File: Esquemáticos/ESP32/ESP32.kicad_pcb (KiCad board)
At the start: 2 copper layers, 100 x 100 mm, 71 parts, among them J1 Conector para bobinas del mot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, J2 Conector para bobinas del mot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, J3 Barrel_Jack, J4 USB Programador, Q1 S8550, Q2 S8550, Q3 S8550, Q4 S8550, Q5 S8550, Q6 S8550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

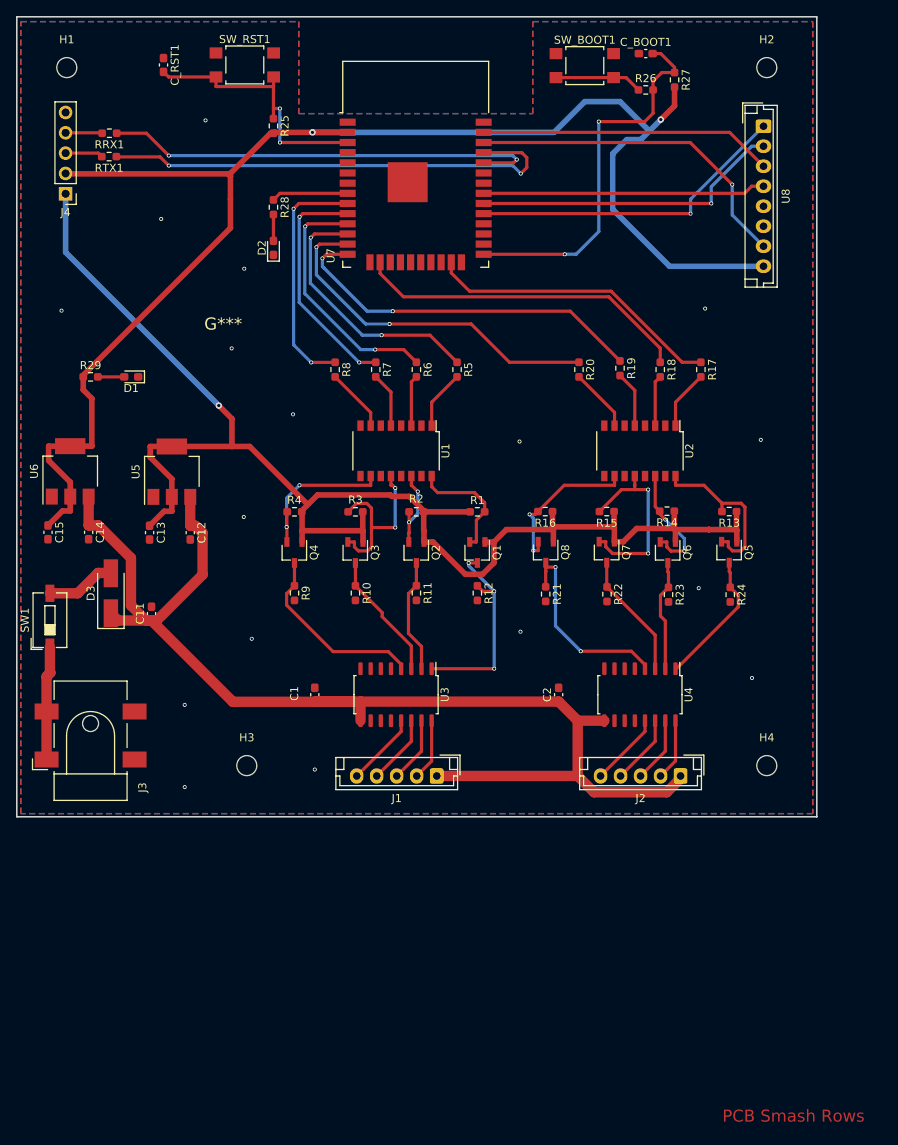
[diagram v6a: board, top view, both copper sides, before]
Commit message: Actualizada la PCB con impresiones de qué es cada pin de los conectores
Pendiente: Agregar capacitor de bypass en la entrada de 3v3 del ESP32 y listo, a comerciar con los chinos
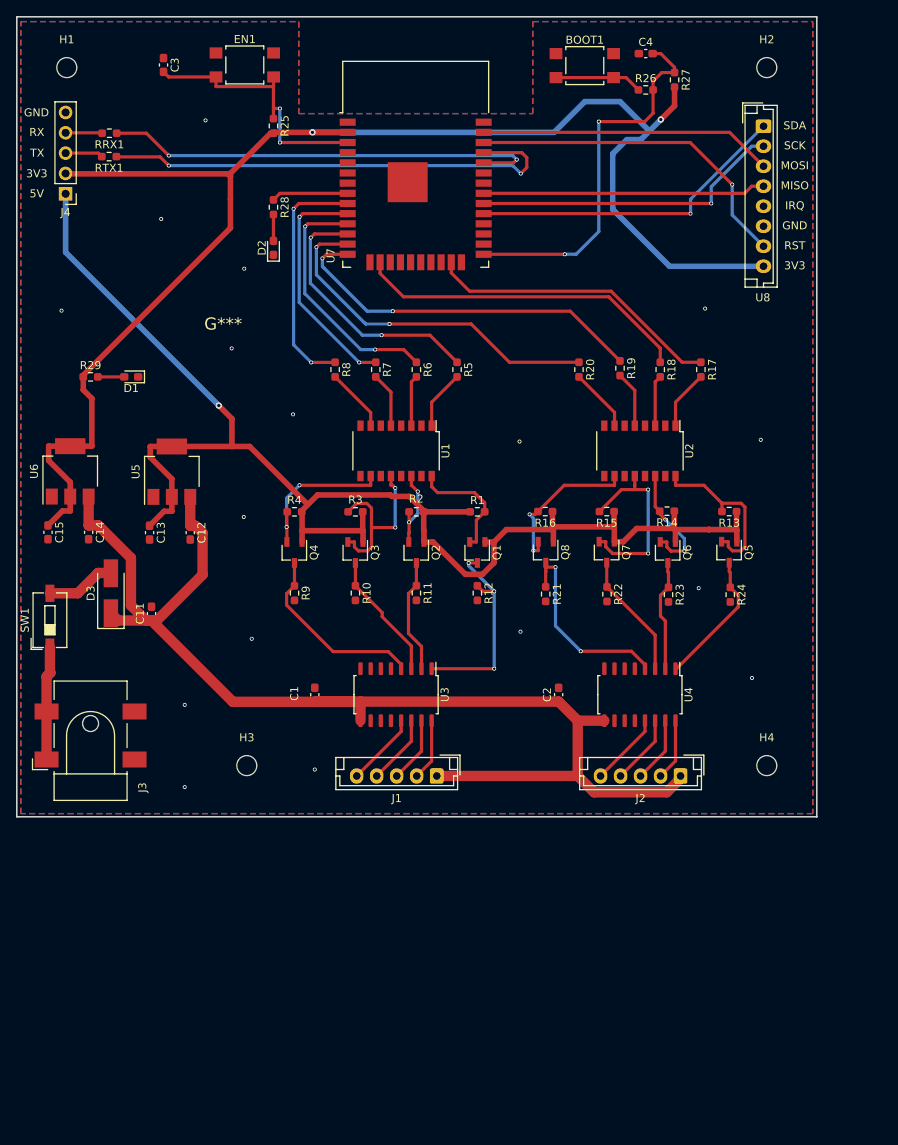
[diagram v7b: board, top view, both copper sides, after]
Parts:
- renumbered SW_BOOT1 to BOOT1, C_RST1 to C3, C_BOOT1 to C4, SW_RST1 to EN1
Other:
- board text added: "3V3"
- board text added: "5V"
- board text added: "GND"
- board text added: "IRQ"
- board text added: "MISO"
- board text added: "MOSI"
- board text added: "RST"
- board text added: "RX"
- board text added: "SCK"
- board text added: "SDA"
- board text added: "TX"
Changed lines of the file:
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@@
     (property "Sheetname" "RFID")
     (attr through_hole)
-    (fp_text reference "U8" (at 8.75 -2.8 90) (layer "F.SilkS")
+    (fp_text reference "U8" (at 21.42 0.09 180) (layer "F.SilkS")
       (effects (font (size 1 1) (thickness 0.15)))
     )
@@
       (net 43 "/Motores/In5") (pinfunction "IO15") (pintype "bidirectional"))
     (pad "24" smd rect (at 5.715 9.255 90) (size 2 0.9) (layers "F.Cu" "F.Paste" "F.Mask")
-      (net 77 "unconnected-(U7-Pad24)") (pinfunction "IO2") (pintype "bidirectional"))
+      (net 77 "unconnected-(U7-Pad24)") (pinfunction "IO2") (pintype "bidirectional+no_connect"))
     (pad "25" smd rect (at 8.5 8.255) (size 2 0.9) (layers "F.Cu" "F.Paste" "F.Mask")
       (net 5 "/Principal/BOOT") (pinfunction "IO0") (pintype "bidirectional"))
     (pad "26" smd rect (at 8.5 6.985) (size 2 0.9) (layers "F.Cu" "F.Paste" "F.Mask")
-      (net 78 "unconnected-(U7-Pad26)") (pinfunction "IO4") (pintype "bidirectional"))
+      (net 78 "unconnected-(U7-Pad26)") (pinfunction "IO4") (pintype "bidirectional+no_connect"))
     (pad "27" smd rect (at 8.5 5.715) (size 2 0.9) (layers "F.Cu" "F.Paste" "F.Mask")
-      (net 79 "unconnected-(U7-Pad27)") (pinfunction "IO16") (pintype "bidirectional"))
+      (net 79 "unconnected-(U7-Pad27)") (pinfunction "IO16") (pintype "bidirectional+no_connect"))
     (pad "28" smd rect (at 8.5 4.445) (size 2 0.9) (layers "F.Cu" "F.Paste" "F.Mask")
-      (net 80 "unconnected-(U7-Pad28)") (pinfunction "IO17") (pintype "bidirectional"))
+      (net 80 "unconnected-(U7-Pad28)") (pinfunction "IO17") (pintype "bidirectional+no_connect"))
     (pad "29" smd rect (at 8.5 3.175) (size 2 0.9) (layers "F.Cu" "F.Paste" "F.Mask")
       (net 81 "/Principal/SS") (pinfunction "IO5") (pintype "bidirectional"))
@@
       (net 84 "unconnected-(U7-Pad32)") (pinfunction "NC") (pintype "no_connect"))
     (pad "33" smd rect (at 8.5 -1.905) (size 2 0.9) (layers "F.Cu" "F.Paste" "F.Mask")
-      (net 85 "unconnected-(U7-Pad33)") (pinfunction "IO21") (pintype "bidirectional"))
+      (net 85 "unconnected-(U7-Pad33)") (pinfunction "IO21") (pintype "bidirectional+no_connect"))
     (pad "34" smd rect (at 8.5 -3.175) (size 2 0.9) (layers "F.Cu" "F.Paste" "F.Mask")
       (net 53 "/Principal/RX") (pinfunction "RXD0/IO3") (pintype "bidirectional"))
@@
     (property "Sheetname" "Principal")
     (attr smd)
-    (fp_text reference "C_RST1" (at 0 -1.43 90) (layer "F.SilkS")
+    (fp_text reference "C3" (at 0 -1.43 90) (layer "F.SilkS")
       (effects (font (size 1 1) (thickness 0.15)))
     )
@@
     (property "Sheetname" "Principal")
     (attr smd)
-    (fp_text reference "SW_BOOT1" (at 0 -3.2) (layer "F.SilkS")
+    (fp_text reference "BOOT1" (at 0 -3.2) (layer "F.SilkS")
       (effects (font (size 1 1) (thickness 0.15)))
     )
@@
     (property "Sheetname" "Principal")
     (attr smd)
-    (fp_text reference "SW_RST1" (at 0 -3.2) (layer "F.SilkS")
+    (fp_text reference "EN1" (at 0 -3.2) (layer "F.SilkS")
       (effects (font (size 1 1) (thickness 0.15)))
     )
@@
     (property "Sheetname" "Principal")
     (attr smd)
-    (fp_text reference "C_BOOT1" (at 0 -1.43) (layer "F.SilkS")
+    (fp_text reference "C4" (at 0 -1.43) (layer "F.SilkS")
       (effects (font (size 1 1) (thickness 0.15)))
     )
@@
   )
   (gr_rect (start 100 52.4) (end 200 152.4) (layer "Edge.Cuts") (width 0.2) (fill none))
-  (gr_text "PCB Smash Rows" (at 197.09 189.81) (layer "F.Cu")
+  (gr_text "SDA" (at 197.25 66) (layer "F.SilkS")
+    (effects (font (size 1 1) (thickness 0.15)))
+  )
+  (gr_text "GND" (at 102.46 64.38) (layer "F.SilkS")
+    (effects (font (size 1 1) (thickness 0.15)))
+  )
+  (gr_text "5V" (at 102.5 74.5) (layer "F.SilkS")
+    (effects (font (size 1 1) (thickness 0.15)))
+  )
+  (gr_text "RX" (at 102.5 66.83) (layer "F.SilkS")
+    (effects (font (size 1 1) (thickness 0.15)))
+  )
+  (gr_text "3V3" (at 197.25 83.5) (layer "F.SilkS")
+    (effects (font (size 1 1) (thickness 0.15)))
+  )
+  (gr_text "3V3" (at 102.5 72) (layer "F.SilkS")
+    (effects (font (size 1 1) (thickness 0.15)))
+  )
+  (gr_text "SCK" (at 197.25 68.5) (layer "F.SilkS")
+    (effects (font (size 1 1) (thickness 0.15)))
+  )
+  (gr_text "RST" (at 197.25 81) (layer "F.SilkS")
+    (effects (font (size 1 1) (thickness 0.15)))
+  )
+  (gr_text "MOSI" (at 197.25 71) (layer "F.SilkS")
+    (effects (font (size 1 1) (thickness 0.15)))
+  )
+  (gr_text "GND" (at 197.25 78.5) (layer "F.SilkS")
+    (effects (font (size 1 1) (thickness 0.15)))
+  )
+  (gr_text "IRQ" (at 197.25 76) (layer "F.SilkS")
+    (effects (font (size 1 1) (thickness 0.15)))
+  )
+  (gr_text "MISO" (at 197.25 73.5) (layer "F.SilkS")
+    (effects (font (size 1 1) (thickness 0.15)))
+  )
+  (gr_text "TX" (at 102.55 69.42) (layer "F.SilkS")
+    (effects (font (size 1 1) (thickness 0.15)))
+  )
+  (gr_text "PCB Smash Rows" (at 197.09 189.81) (layer "Cmts.User")
     (effects (font (size 1.5 1.5) (thickness 0.3)))
   )

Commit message: Placa con Logo
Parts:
- removed the G*** at (125.8, 90.8)
- added G***: LOGO, LibraryLogo:LogoSR, F.Cu at (125.8, 119.4)
